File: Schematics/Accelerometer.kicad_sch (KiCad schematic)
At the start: 3 parts, among them U7 H3LIS100DL

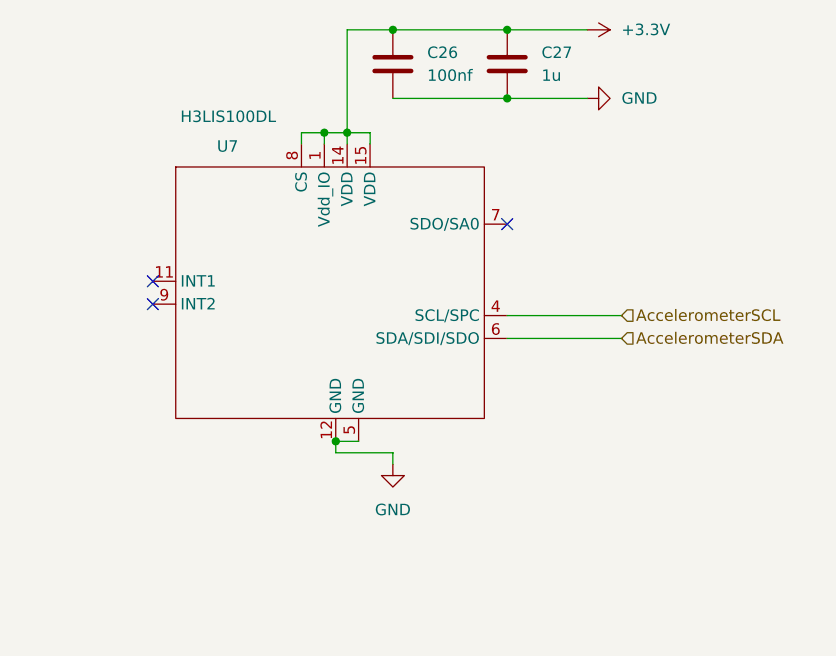
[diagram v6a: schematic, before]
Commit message: first layout need to go over schematic
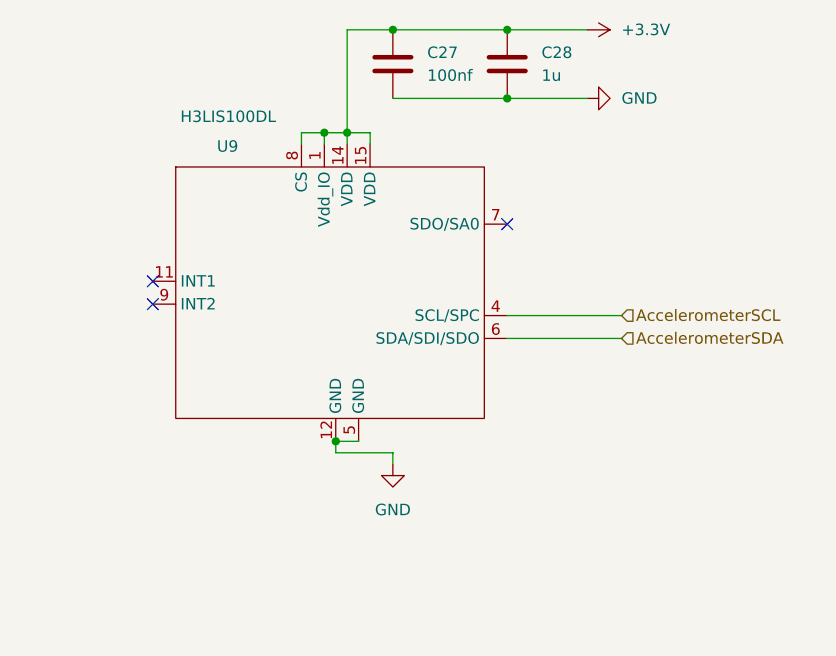
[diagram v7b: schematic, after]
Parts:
- renumbered C26 to C27, C27 to C28, U7 to U9
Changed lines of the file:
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@@
 		(dnp no)
 		(fields_autoplaced yes)
-		(property "Reference" "C26"
+		(property "Reference" "C27"
 			(at 160.02 81.2799 0)
 			(effects
@@
 			(project ""
 				(path "/6cb3dda3-5fe8-4715-b831-354360aa3199/845ef161-5bd7-4496-b5c2-e65e4f30444a"
-					(reference "C26")
+					(reference "C27")
 					(unit 1)
 				)
@@
 		(on_board yes)
 		(dnp no)
-		(property "Reference" "U7"
+		(property "Reference" "U9"
 			(at 136.652 91.694 0)
 			(effects
@@
 			(project ""
 				(path "/6cb3dda3-5fe8-4715-b831-354360aa3199/845ef161-5bd7-4496-b5c2-e65e4f30444a"
-					(reference "U7")
+					(reference "U9")
 					(unit 1)
 				)
@@
 		(dnp no)
 		(fields_autoplaced yes)
-		(property "Reference" "#PWR080"
+		(property "Reference" "#PWR091"
 			(at 184.15 86.36 0)
 			(effects
@@
 			(project ""
 				(path "/6cb3dda3-5fe8-4715-b831-354360aa3199/845ef161-5bd7-4496-b5c2-e65e4f30444a"
-					(reference "#PWR080")
+					(reference "#PWR091")
 					(unit 1)
 				)
@@
 		(dnp no)
 		(fields_autoplaced yes)
-		(property "Reference" "#PWR078"
+		(property "Reference" "#PWR089"
 			(at 156.21 133.35 0)
 			(effects
@@
 			(project "flightcomputer2"
 				(path "/6cb3dda3-5fe8-4715-b831-354360aa3199/845ef161-5bd7-4496-b5c2-e65e4f30444a"
-					(reference "#PWR078")
+					(reference "#PWR089")
 					(unit 1)
 				)
@@
 		(dnp no)
 		(fields_autoplaced yes)
-		(property "Reference" "C27"
+		(property "Reference" "C28"
 			(at 172.72 81.2799 0)
 			(effects
@@
 			(project "flightcomputer2"
 				(path "/6cb3dda3-5fe8-4715-b831-354360aa3199/845ef161-5bd7-4496-b5c2-e65e4f30444a"
-					(reference "C27")
+					(reference "C28")
 					(unit 1)
 				)
@@
 		(dnp no)
 		(fields_autoplaced yes)
-		(property "Reference" "#PWR079"
+		(property "Reference" "#PWR090"
 			(at 173.99 78.74 0)
 			(effects
@@
 			(project "flightcomputer2"
 				(path "/6cb3dda3-5fe8-4715-b831-354360aa3199/845ef161-5bd7-4496-b5c2-e65e4f30444a"
-					(reference "#PWR079")
+					(reference "#PWR090")
 					(unit 1)
 				)
